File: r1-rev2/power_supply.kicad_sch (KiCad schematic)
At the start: 29 parts, among them J5 GT-BTP30003-xxxA-16A, J8 BATT, Q3 AO3401A, U4 LM66100DCK, U5 TPS62A01DRLR, U6 TPS62A01DRLR, U7 AP2125K-3.0, U8 AP2125K-3.0, U9 TP4057

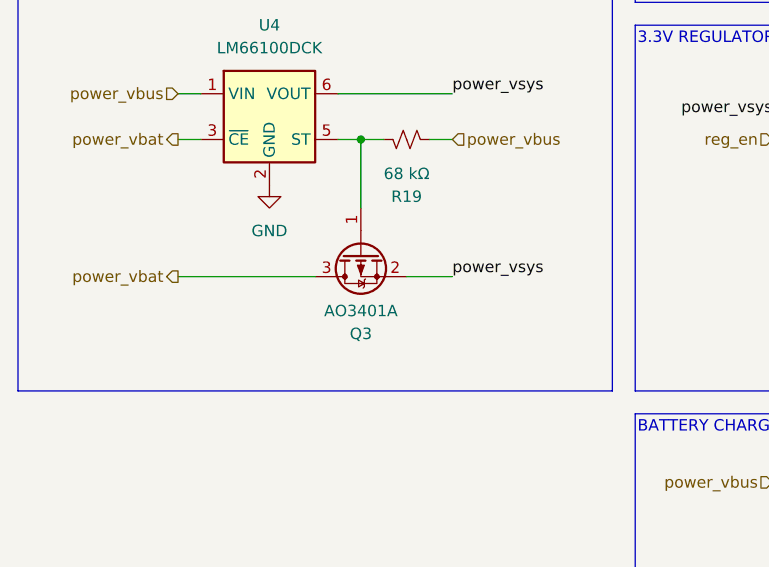
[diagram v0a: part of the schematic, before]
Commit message: Fix symbol library links & resync footprints from KiCAD libraries
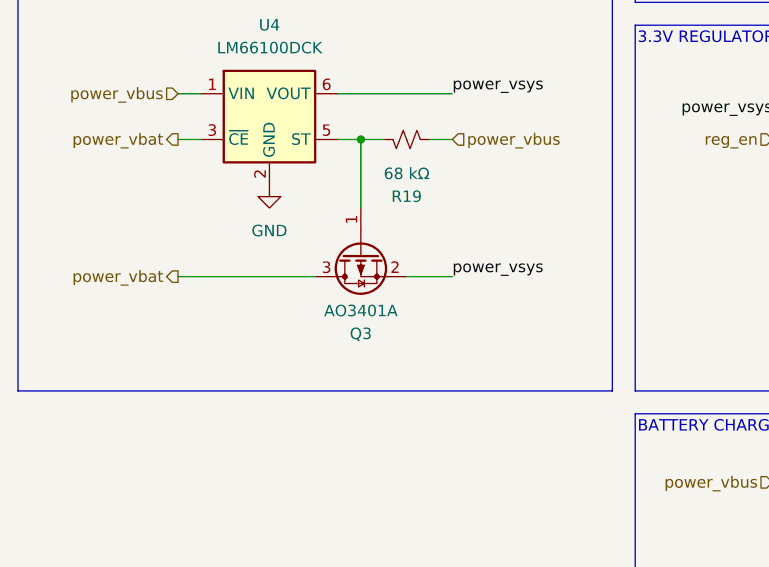
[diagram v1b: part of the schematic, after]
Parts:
- Q3: symbol Device:Q_PMOS_GSD -> Transistor_FET:Q_PMOS_GSD
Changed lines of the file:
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@@
 	)
 	(symbol
-		(lib_id "Device:Q_PMOS_GSD")
+		(lib_id "Transistor_FET:Q_PMOS_GSD")
 		(at 68.58 101.6 90)
 		(mirror x)
